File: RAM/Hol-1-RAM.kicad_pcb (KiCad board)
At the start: 2 copper layers, 109.2 x 81.3 mm, 22 parts, among them P1 ADDRESS PORT, P2 DATA PORT, P3 DATA BUS, P4 Power, U1 74LS139, U10 74LS04, U11 74LS04, U12 74LS245, U2 74LS189, U3 74LS189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

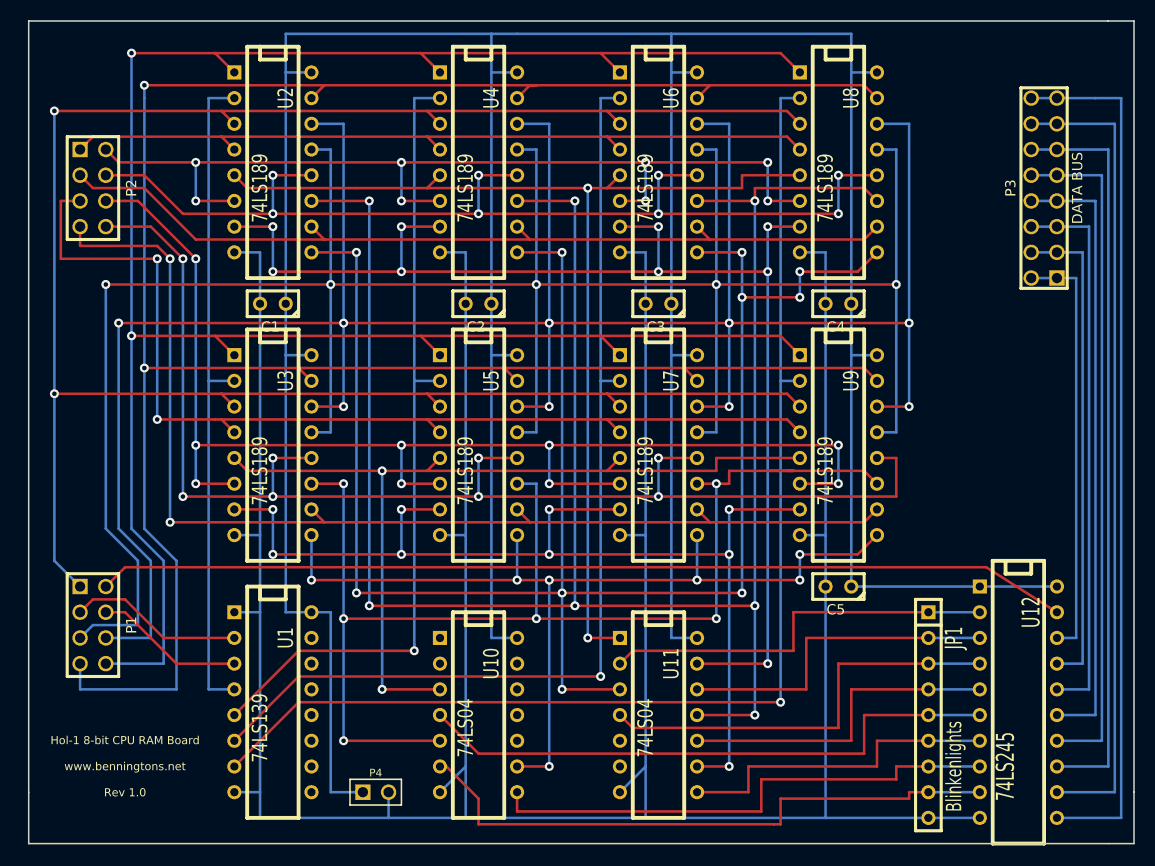
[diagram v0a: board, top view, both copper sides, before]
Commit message: v1.0.2 reduced RAM board from 31 to 30 rows to match perfboard
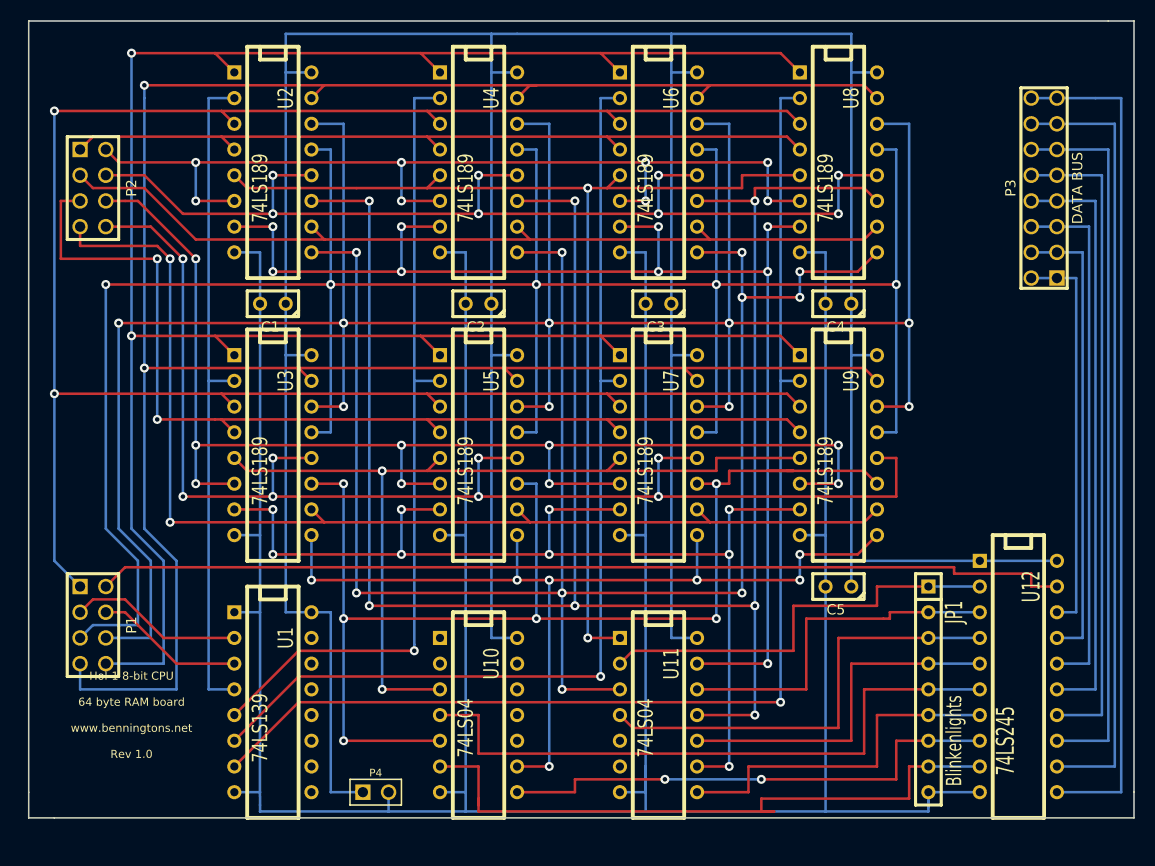
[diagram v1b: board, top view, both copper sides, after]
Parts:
- moved JP1 2.54 mm to (193.0, 129.5)
- moved U12 2.54 mm to (201.9, 128.3)
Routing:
- net N-0000038: track 60.4 -> 65.4 mm
- net N-0000028: track 58.7 -> 63.5 mm
- net GND: track 329.8 -> 333.0 mm
- net N-0000050: track 61.0 -> 58.4 mm
- net N-0000049: track 86.4 -> 83.8 mm
- net N-0000054: track 48.3 -> 45.7 mm
- net N-0000044: track 42.4 -> 45.0 mm
- net N-0000042: track 39.9 -> 42.4 mm
- net N-0000055: track 54.6 -> 52.1 mm
- net N-0000053: track 41.9 -> 39.4 mm
- net N-0000048: track 80.0 -> 77.5 mm
- net N-0000047: track 73.7 -> 71.1 mm
- net N-0000046: track 67.3 -> 64.8 mm
- net N-0000043: track 33.0 -> 35.6 mm
- net N-0000041: track 33.0 -> 35.6 mm
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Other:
- board size 109.2 x 81.3 mm -> 109.2 x 78.7 mm
- board text added: "Hol-1 8-bit CPU 64 byte RAM board www.benningtons.net Rev 1.0"
- board text removed: "Hol-1 8-bit CPU RAM Board www.benningtons.net Rev 1.0"
